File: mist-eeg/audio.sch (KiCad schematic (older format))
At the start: 29 parts, among them J3 Audio, U10 ADAU1372

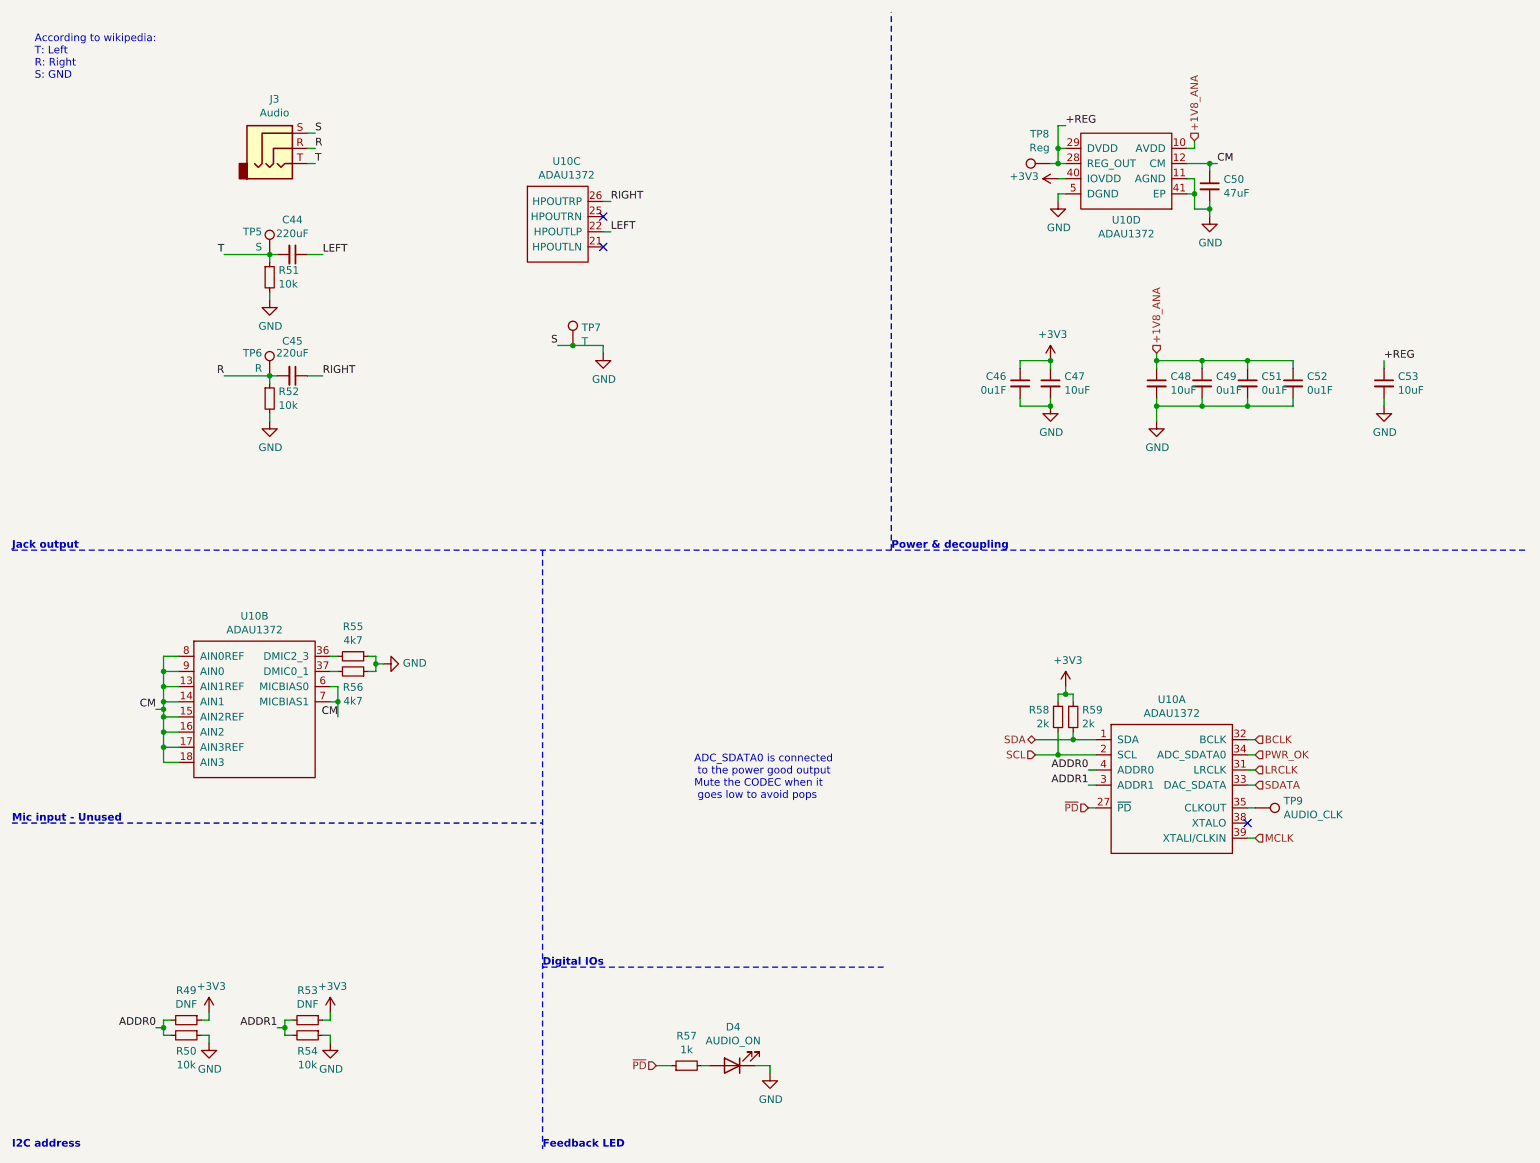
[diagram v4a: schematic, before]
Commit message: Change buckboost regulator used
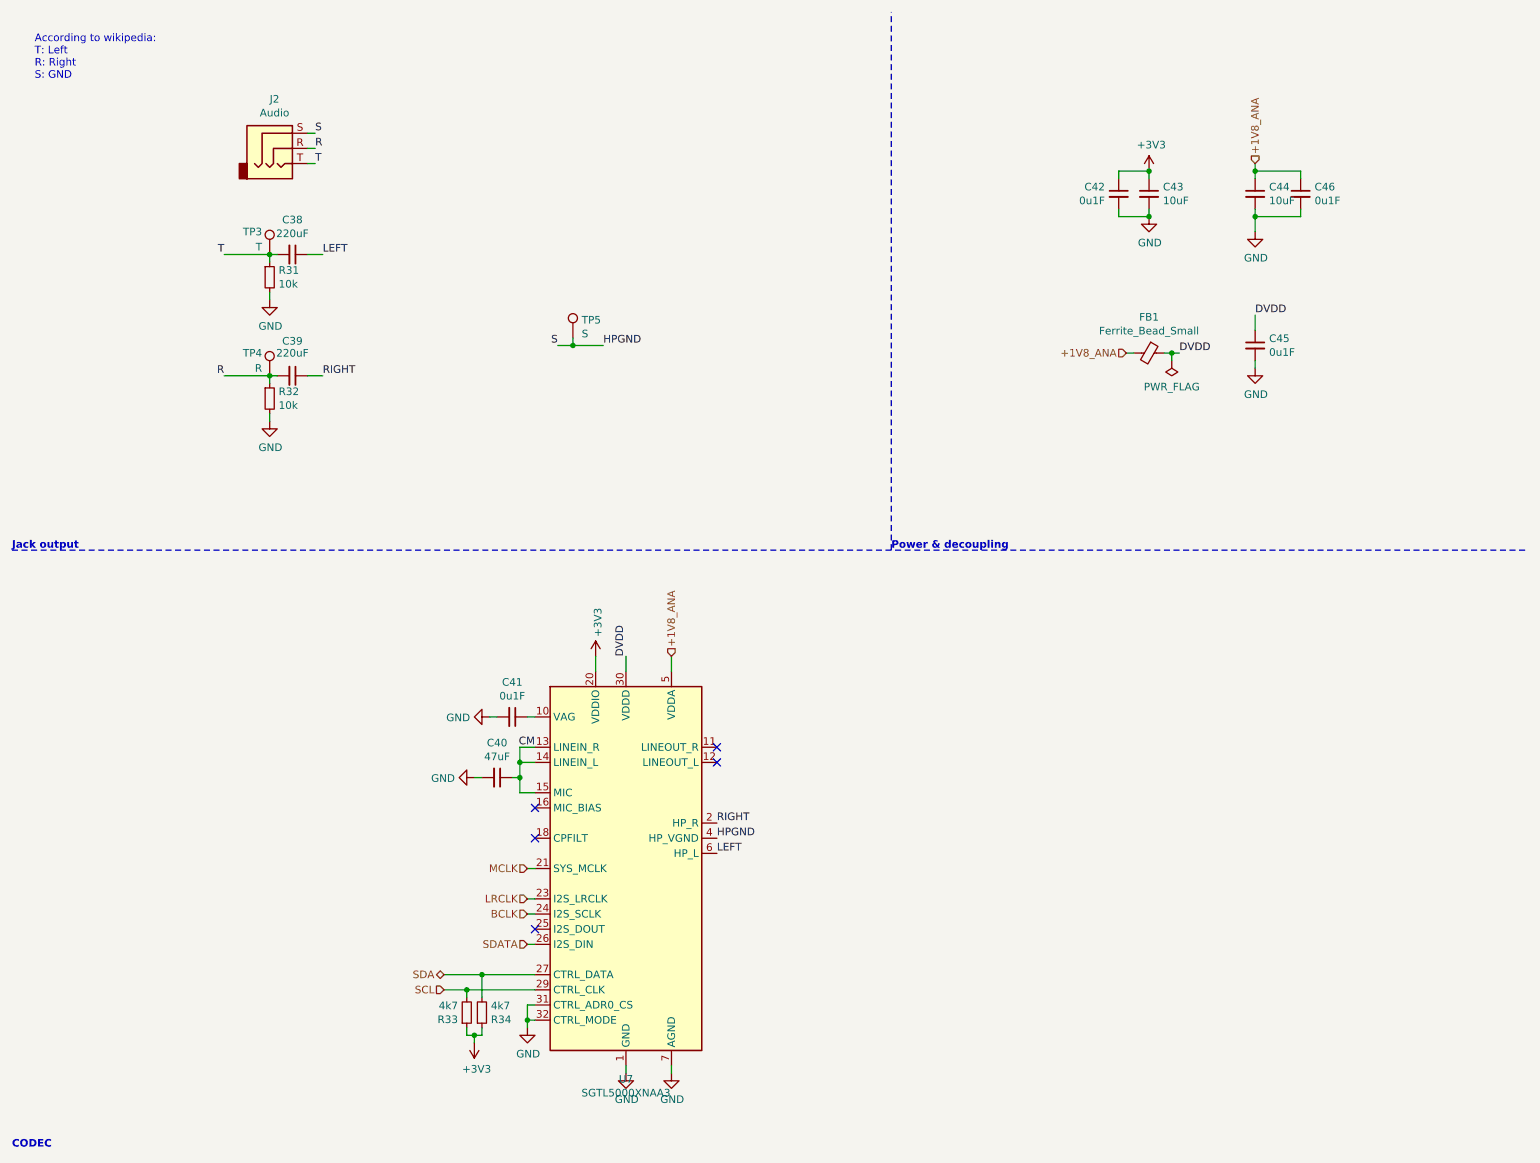
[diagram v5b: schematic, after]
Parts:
- removed C53: 10uF, Capacitor_SMD:C_0603_1608Metric, symbol Device:C_Small
- removed D4: AUDIO_ON, LED_SMD:LED_0603_1608Metric, symbol Device:LED
- removed R49, R53: DNF, Resistor_SMD:R_0603_1608Metric, symbol Device:R_Small
- removed R50, R54: 10k, Resistor_SMD:R_0603_1608Metric, symbol Device:R_Small
- removed R55, R56: 4k7, Resistor_SMD:R_0201_0603Metric, symbol Device:R_Small
- removed R57: 1k, Resistor_SMD:R_0402_1005Metric, symbol Device:R_Small
- removed TP8: Reg, TestPoint:TestPoint_Pad_D1.0mm, symbol Connector:TestPoint
- removed TP9: AUDIO_CLK, TestPoint:TestPoint_Pad_D1.0mm, symbol Connector:TestPoint
- removed U10: ADAU1372, Package_DFN_QFN:QFN-40-1EP_6x6mm_P0.5mm_EP4.6x4.6mm, symbol components:ADAU1372
- added FB1: Ferrite_Bead_Small, Resistor_SMD:R_0603_1608Metric, symbol Device:Ferrite_Bead_Small
- added U7: SGTL5000XNAA3, Package_DFN_QFN:QFN-32-1EP_5x5mm_P0.5mm_EP3.6x3.6mm, symbol Audio:SGTL5000XNAA3
- R33: renamed from R58; value 2k -> 4k7
- R34: renamed from R59; value 2k -> 4k7
- TP3: renamed from TP5; value S -> T
- TP5: renamed from TP7; value T -> S
- renumbered C44 to C38, C45 to C39, C50 to C40, C52 to C41, C46 to C42, C47 to C43, C48 to C44, C51 to C45, C49 to C46, J3 to J2, R51 to R31, R52 to R32, TP6 to TP4
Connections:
- net +1V8_ANA: now also FB1.2, U7.5 (VDDA); no longer C41.1, C45.1
- net +3V3: now also U7.20 (VDDIO)
- net BCLK: now also U7.24 (I2S_SCLK)
- net CM: now also U7.13 (LINEIN_R), U7.14 (LINEIN_L), U7.15 (MIC)
- net GND: now also U7.1 (GND), U7.3 (GND), U7.31 (CTRL_ADR0_CS), U7.32 (CTRL_MODE), U7.33 (GND), U7.7 (AGND); no longer J2.S, TP5.1
- net LEFT: now also U7.6 (HP_L)
- net LRCLK: now also U7.23 (I2S_LRCLK)
- net MCLK: now also U7.21 (SYS_MCLK)
- net RIGHT: now also U7.2 (HP_R)
- net SCL: now also U7.29 (CTRL_CLK)
- net SDA: now also U7.27 (CTRL_DATA)
- net SDATA: now also U7.26 (I2S_DIN)
- new net: C41.1, U7.10 (VAG)
- new net DVDD: C45.1, FB1.1, U7.30 (VDDD)
- new net HPGND: J2.S, TP5.1, U7.4 (HP_VGND)
- no-connect marks 3 -> 5
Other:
- note added: "CODEC"
- note removed: "ADC_SDATA0 is connected\n to the power good output\nMute the CODEC when it\n goes low to avoid pops"
- note removed: "Digital IOs"
- note removed: "Feedback LED"
- note removed: "I2C address"
- note removed: "Mic input - Unused"
- moved on the sheet: C40, C41, C42, C43, C44, C45, C46, R33, R34, TP5

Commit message: Switch to POL switching regulator to accelerate production of the board
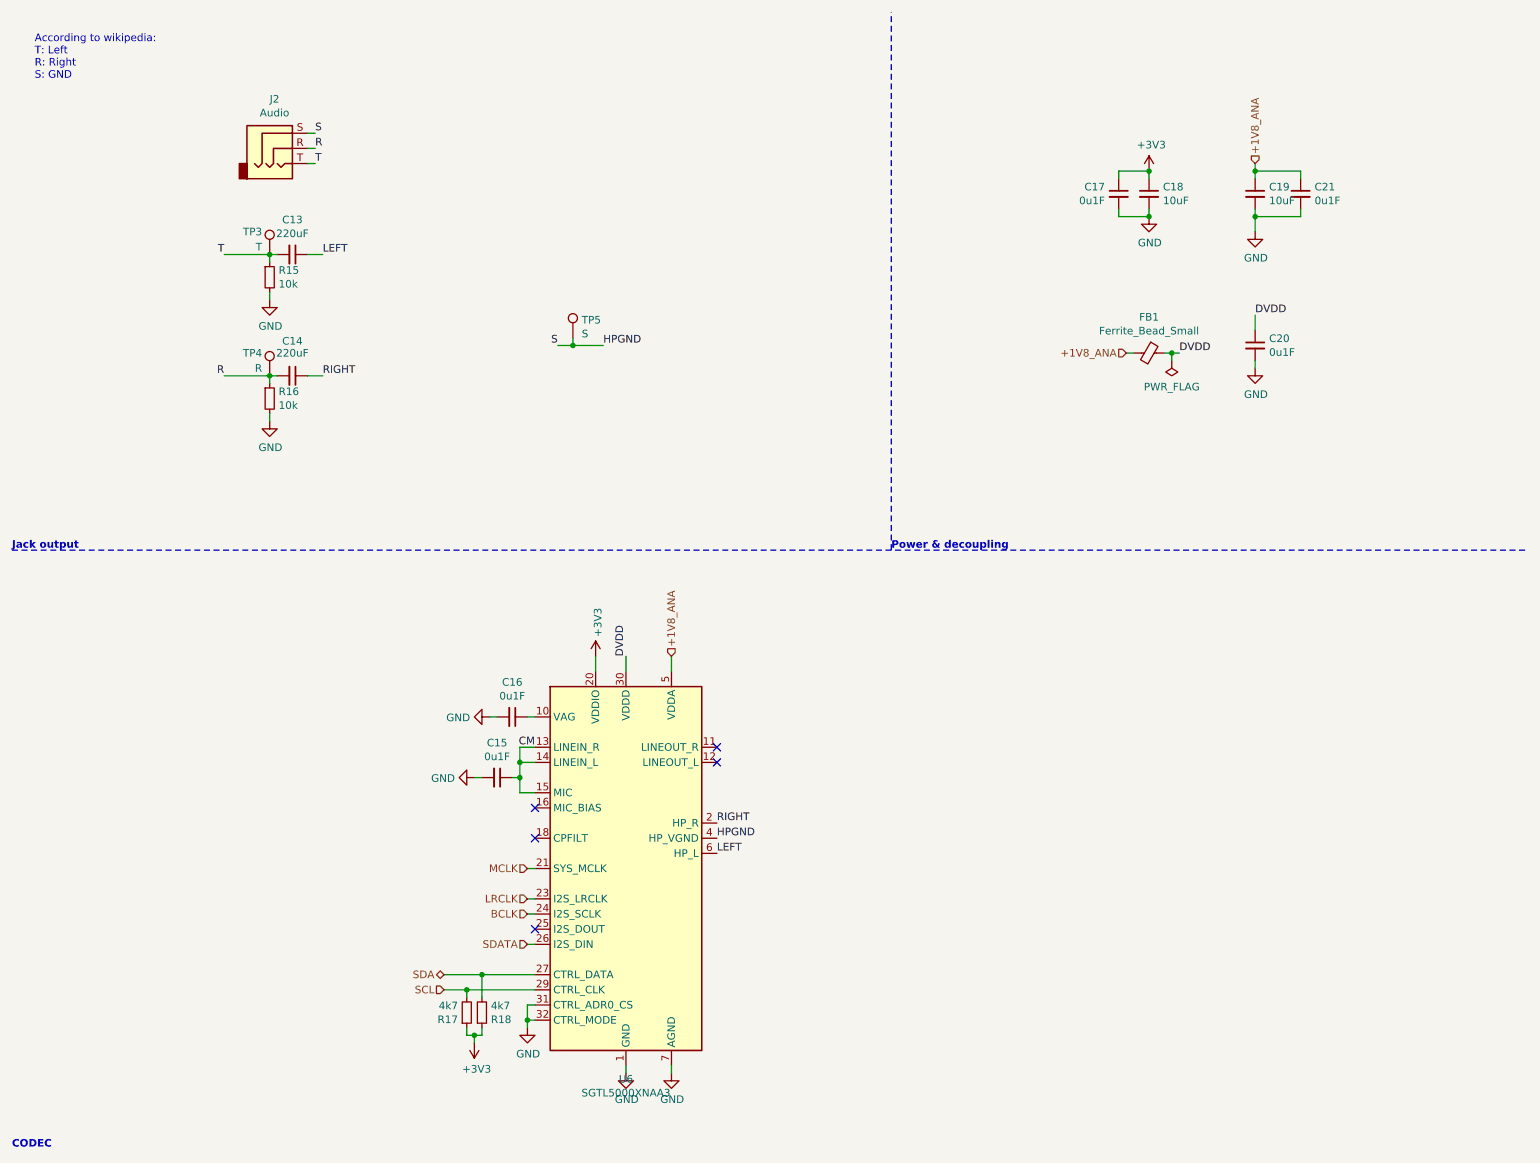
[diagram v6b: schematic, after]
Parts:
- removed C40: 47uF, Capacitor_SMD:C_1210_3225Metric, symbol Device:C_Small
- added C15: 0u1F, Capacitor_SMD:C_0201_0603Metric, symbol Device:C_Small
- renumbered C38 to C13, C39 to C14, C41 to C16, C42 to C17, C43 to C18, C44 to C19, C45 to C20, C46 to C21, R31 to R15, R32 to R16, R33 to R17, R34 to R18, U7 to U6
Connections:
- net CM: now also C15.1
- net GND: now also C15.2
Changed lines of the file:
@@
 $Descr USLetter 11000 8500
 encoding utf-8
-Sheet 7 11
+Sheet 4 8
 Title "Portiloop"
-Date "2021-08-03"
-Rev "1D"
+Date "2021-08-05"
+Rev "1E"
 Comp "MIST Lab"
 Comment1 "Designed by Xavier L'Heureux"
@@
 	2500 1300 2450 1300
 $Comp
-L Device:C_Small C38
+L Device:C_Small C13
 U 1 1 60ABF165
 P 2350 2100
-F 0 "C38" V 2121 2100 50  0000 C CNN
+F 0 "C13" V 2121 2100 50  0000 C CNN
 F 1 "220uF" V 2212 2100 50  0000 C CNN
 F 2 "Capacitor_SMD:C_1210_3225Metric" H 2350 2100 50  0001 C CNN
@@
 $EndComp
 $Comp
-L Device:R_Small R31
+L Device:R_Small R15
 U 1 1 60ABF5BC
 P 2200 2250
-F 0 "R31" H 2259 2296 50  0000 L CNN
+F 0 "R15" H 2259 2296 50  0000 L CNN
 F 1 "10k" H 2259 2205 50  0000 L CNN
 F 2 "Resistor_SMD:R_0603_1608Metric" H 2200 2250 50  0001 C CNN
@@
 RIGHT
 $Comp
-L Device:C_Small C39
+L Device:C_Small C14
 U 1 1 60AC80C1
 P 2350 2900
-F 0 "C39" V 2121 2900 50  0000 C CNN
+F 0 "C14" V 2121 2900 50  0000 C CNN
 F 1 "220uF" V 2200 2900 50  0000 C CNN
 F 2 "Capacitor_SMD:C_1210_3225Metric" H 2350 2900 50  0001 C CNN
@@
 $EndComp
 $Comp
-L Device:R_Small R32
+L Device:R_Small R16
 U 1 1 60AC80C7
 P 2200 3050
-F 0 "R32" H 2259 3096 50  0000 L CNN
+F 0 "R16" H 2259 3096 50  0000 L CNN
 F 1 "10k" H 2259 3005 50  0000 L CNN
 F 2 "Resistor_SMD:R_0603_1608Metric" H 2200 3050 50  0001 C CNN
@@
 Text Notes 500  4050 0    50   ~ 10
 Jack output
-$Comp
-L Device:C_Small C40
-U 1 1 60ADB2B1
-P 3700 5550
-F 0 "C40" V 3471 5550 50  0000 C CNN
-F 1 "47uF" V 3562 5550 50  0000 C CNN
-F 2 "Capacitor_SMD:C_1210_3225Metric" H 3700 5550 50  0001 C CNN
-F 3 "~" H 3700 5550 50  0001 C CNN
-	1    3700 5550
-	0    1    1    0
-$EndComp
 Text HLabel 4850 4750 1    50   Input ~ 0
 +1V8_ANA
@@
 SCL
 $Comp
-L Device:R_Small R34
+L Device:R_Small R18
 U 1 1 60B0947B
 P 3600 7100
-F 0 "R34" H 3659 7146 50  0000 L CNN
+F 0 "R18" H 3659 7146 50  0000 L CNN
 F 1 "4k7" H 3659 7055 50  0000 L CNN
 F 2 "Resistor_SMD:R_0201_0603Metric" H 3600 7100 50  0001 C CNN
@@
 $EndComp
 $Comp
-L Device:R_Small R33
+L Device:R_Small R17
 U 1 1 60B0B8D0
 P 3500 7100
-F 0 "R33" H 3442 7146 50  0000 R CNN
+F 0 "R17" H 3442 7146 50  0000 R CNN
 F 1 "4k7" H 3442 7055 50  0000 R CNN
 F 2 "Resistor_SMD:R_0201_0603Metric" H 3500 7100 50  0001 C CNN
@@
 Power & decoupling
 $Comp
-L power:GND #PWR059
+L power:GND #PWR037
 U 1 1 60C1A59D
 P 8000 1850
-F 0 "#PWR059" H 8000 1600 50  0001 C CNN
+F 0 "#PWR037" H 8000 1600 50  0001 C CNN
 F 1 "GND" H 8005 1677 50  0000 C CNN
 F 2 "" H 8000 1850 50  0001 C CNN
@@
 $EndComp
 $Comp
-L Device:C_Small C43
+L Device:C_Small C18
 U 1 1 60C1ABFC
 P 8000 1700
-F 0 "C43" H 8092 1746 50  0000 L CNN
+F 0 "C18" H 8092 1746 50  0000 L CNN
 F 1 "10uF" H 8092 1655 50  0000 L CNN
 F 2 "Capacitor_SMD:C_0603_1608Metric" H 8000 1700 50  0001 C CNN
@@
 	8000 1600 8000 1550
 $Comp
-L Device:C_Small C44
+L Device:C_Small C19
 U 1 1 60C26CBF
 P 8700 1700
-F 0 "C44" H 8792 1746 50  0000 L CNN
+F 0 "C19" H 8792 1746 50  0000 L CNN
 F 1 "10uF" H 8792 1655 50  0000 L CNN
 F 2 "Capacitor_SMD:C_0603_1608Metric" H 8700 1700 50  0001 C CNN
@@
 	8700 1500 8700 1550
 $Comp
-L Device:C_Small C46
+L Device:C_Small C21
 U 1 1 60C2D5CD
 P 9000 1700
-F 0 "C46" H 9092 1746 50  0000 L CNN
+F 0 "C21" H 9092 1746 50  0000 L CNN
 F 1 "0u1F" H 9092 1655 50  0000 L CNN
 F 2 "Capacitor_SMD:C_0201_0603Metric" H 9000 1700 50  0001 C CNN
@@
 $EndComp
 $Comp
-L Device:C_Small C45
+L Device:C_Small C20
 U 1 1 60C2D731
 P 8700 2700
-F 0 "C45" H 8792 2746 50  0000 L CNN
+F 0 "C20" H 8792 2746 50  0000 L CNN
 F 1 "0u1F" H 8792 2655 50  0000 L CNN
 F 2 "Capacitor_SMD:C_0201_0603Metric" H 8700 2700 50  0001 C CNN
@@
 $EndComp
 $Comp
-L Device:C_Small C41
+L Device:C_Small C16
 U 1 1 60C2D8BB
 P 3800 5150
-F 0 "C41" V 3571 5150 50  0000 C CNN
+F 0 "C16" V 3571 5150 50  0000 C CNN
 F 1 "0u1F" V 3662 5150 50  0000 C CNN
 F 2 "Capacitor_SMD:C_0201_0603Metric" H 3800 5150 50  0001 C CNN
@@
 	500  4050 10500 4050
 $Comp
-L power:GND #PWR060
+L power:GND #PWR038
 U 1 1 611D9111
 P 8700 1950
-F 0 "#PWR060" H 8700 1700 50  0001 C CNN
+F 0 "#PWR038" H 8700 1700 50  0001 C CNN
 F 1 "GND" H 8705 1777 50  0000 C CNN
 F 2 "" H 8700 1950 50  0001 C CNN
@@
 $EndComp
 $Comp
-L power:GND #PWR050
+L power:GND #PWR027
 U 1 1 611DC98D
 P 2200 2400
-F 0 "#PWR050" H 2200 2150 50  0001 C CNN
+F 0 "#PWR027" H 2200 2150 50  0001 C CNN
 F 1 "GND" H 2205 2227 50  0000 C CNN
 F 2 "" H 2200 2400 50  0001 C CNN
@@
 $EndComp
 $Comp
-L power:GND #PWR051
+L power:GND #PWR028
 U 1 1 611DCDAF
 P 2200 3200
-F 0 "#PWR051" H 2200 2950 50  0001 C CNN
+F 0 "#PWR028" H 2200 2950 50  0001 C CNN
 F 1 "GND" H 2205 3027 50  0000 C CNN
 F 2 "" H 2200 3200 50  0001 C CNN
@@
 	4100 2700 4200 2700
 $Comp
-L Device:C_Small C42
+L Device:C_Small C17
 U 1 1 60D754E8
 P 7800 1700
-F 0 "C42" H 7709 1746 50  0000 R CNN
+F 0 "C17" H 7709 1746 50  0000 R CNN
 F 1 "0u1F" H 7709 1655 50  0000 R CNN
 F 2 "Capacitor_SMD:C_0201_0603Metric" H 7800 1700 50  0001 C CNN
@@
 CM
 $Comp
-L power:+3V3 #PWR058
+L power:+3V3 #PWR036
 U 1 1 61142B16
 P 8000 1550
-F 0 "#PWR058" H 8000 1400 50  0001 C CNN
+F 0 "#PWR036" H 8000 1400 50  0001 C CNN
 F 1 "+3V3" H 8015 1723 50  0000 C CNN
 F 2 "" H 8000 1550 50  0001 C CNN
@@
 $EndComp
 $Comp
-L power:+3V3 #PWR053
+L power:+3V3 #PWR030
 U 1 1 611790DA
 P 3550 7300
-F 0 "#PWR053" H 3550 7150 50  0001 C CNN
+F 0 "#PWR030" H 3550 7150 50  0001 C CNN
 F 1 "+3V3" H 3565 7473 50  0000 C CNN
 F 2 "" H 3550 7300 50  0001 C CNN
@@
 $EndComp
 $Comp
-L power:+3V3 #PWR055
+L power:+3V3 #PWR033
 U 1 1 611B1AA0
 P 4350 4750
-F 0 "#PWR055" H 4350 4600 50  0001 C CNN
+F 0 "#PWR033" H 4350 4600 50  0001 C CNN
 F 1 "+3V3" V 4365 4878 50  0000 L CNN
 F 2 "" H 4350 4750 50  0001 C CNN
@@
 	8700 2500 8700 2600
 $Comp
-L power:GND #PWR061
+L power:GND #PWR039
 U 1 1 610F8854
 P 8700 2850
-F 0 "#PWR061" H 8700 2600 50  0001 C CNN
+F 0 "#PWR039" H 8700 2600 50  0001 C CNN
 F 1 "GND" H 8705 2677 50  0000 C CNN
 F 2 "" H 8700 2850 50  0001 C CNN
@@
 	4200 2650 4200 2700
 $Comp
-L power:GND #PWR054
+L power:GND #PWR031
 U 1 1 61146BA2
 P 3650 5150
-F 0 "#PWR054" H 3650 4900 50  0001 C CNN
+F 0 "#PWR031" H 3650 4900 50  0001 C CNN
 F 1 "GND" V 3655 5022 50  0000 R CNN
 F 2 "" H 3650 5150 50  0001 C CNN
@@
 	3950 6150 3900 6150
 $Comp
-L power:GND #PWR057
+L power:GND #PWR035
 U 1 1 61178271
 P 4850 7500
-F 0 "#PWR057" H 4850 7250 50  0001 C CNN
+F 0 "#PWR035" H 4850 7250 50  0001 C CNN
 F 1 "GND" H 4855 7327 50  0000 C CNN
 F 2 "" H 4850 7500 50  0001 C CNN
@@
 NoConn ~ 3950 5750
 $Comp
-L power:GND #PWR052
+L power:GND #PWR029
 U 1 1 6117F384
 P 3550 5550
-F 0 "#PWR052" H 3550 5300 50  0001 C CNN
+F 0 "#PWR029" H 3550 5300 50  0001 C CNN
 F 1 "GND" V 3555 5422 50  0000 R CNN
 F 2 "" H 3550 5550 50  0001 C CNN
@@
 	8150 2750 8200 2750
 $Comp
-L Audio:SGTL5000XNAA3 U7
+L Audio:SGTL5000XNAA3 U6
 U 1 1 612C7288
 P 4550 6150
-F 0 "U7" H 4550 4761 50  0000 C CNN
+F 0 "U6" H 4550 4761 50  0000 C CNN
 F 1 "SGTL5000XNAA3" H 4550 4670 50  0000 C CNN
 F 2 "Package_DFN_QFN:QFN-32-1EP_5x5mm_P0.5mm_EP3.6x3.6mm" H 4550 6150 50  0001 C CNN
@@
 	3600 6850 3950 6850
 $Comp
-L power:GND #PWR056
+L power:GND #PWR034
 U 1 1 612DB80F
 P 4550 7500
-F 0 "#PWR056" H 4550 7250 50  0001 C CNN
+F 0 "#PWR034" H 4550 7250 50  0001 C CNN
 F 1 "GND" H 4555 7327 50  0000 C CNN
 F 2 "" H 4550 7500 50  0001 C CNN
@@
 NoConn ~ 3950 5950
 $Comp
-L power:GND #PWR0119
+L power:GND #PWR032
 U 1 1 61153E17
 P 3900 7200
-F 0 "#PWR0119" H 3900 6950 50  0001 C CNN
+F 0 "#PWR032" H 3900 6950 50  0001 C CNN
 F 1 "GND" H 3905 7027 50  0000 C CNN
 F 2 "" H 3900 7200 50  0001 C CNN
@@
 Wire Wire Line
 	3900 7150 3900 7050
+$Comp
+L Device:C_Small C15
+U 1 1 611B4568
+P 3700 5550
+F 0 "C15" V 3471 5550 50  0000 C CNN
+F 1 "0u1F" V 3562 5550 50  0000 C CNN
+F 2 "Capacitor_SMD:C_0201_0603Metric" H 3700 5550 50  0001 C CNN
+F 3 "~" H 3700 5550 50  0001 C CNN
+	1    3700 5550
+	0    1    1    0
+$EndComp
 $EndSCHEMATC
